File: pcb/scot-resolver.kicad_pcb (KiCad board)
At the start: 2 copper layers, 108.6 x 79.4 mm, 149 parts, among them IC1 AD8692ARMZ, IC10 AD2S1210, IC2 AD8397ARZ, IC3 AD8692ARMZ, IC4 TSR1, IC5 AD8692ARMZ, IC6 AD8692ARMZ, IC7 AD8692ARMZ, IC8 MCP2562, IC9 STM32F0xxKxTx, J1 Conn_01x02_Female, J2 Conn_01x02_Female, J3 Conn_01x02_Female, J4 Conn_01x03_Female, J5 Conn_01x03_Female, J6 Conn_01x03_Female, J7 CONN_01x03, P1 SWD, U1 MCP1703A-5002_SOT223, U2 LT1762, U3 MCP1703A-5002_SOT223, U4 MCP1703A-5002_SOT223, U5 MCP1703A-3302_SOT223, Y1 Crystal_GND24, Y2 Crystal

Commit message: pcb: WIP layout of v2.
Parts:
- removed C40, C52: 6n8, Capacitor_SMD:C_0402_1005Metric
- removed C47: 1u, Capacitor_SMD:C_0603_1608Metric_Pad1.05x0.95mm_HandSolder
- removed C48, C49: 100n, Capacitor_SMD:C_0402_1005Metric
- removed C50: 1n2, Capacitor_SMD:C_0402_1005Metric
- removed C51: 220p, Capacitor_SMD:C_0402_1005Metric
- removed D1: D, Diode_SMD:D_1206_3216Metric_Pad1.42x1.75mm_HandSolder
- removed IC5, IC7: AD8692ARMZ, agg:MSOP-8
- removed R23, R33: 2K, Resistor_SMD:R_0402_1005Metric
- removed R24, R34: 22K, Resistor_SMD:R_0402_1005Metric
- removed R25, R35: 4K7, Resistor_SMD:R_0402_1005Metric
- removed R31: 27K, Resistor_SMD:R_0402_1005Metric
- removed R32: 1K2, Resistor_SMD:R_0402_1005Metric
- added FB5: 600R@100M/1A, Inductor_SMD:L_0805_2012Metric_Pad1.15x1.40mm_HandSolder, F.Cu at (219.6, 133.6)
- added FB6: 600R@100M/1A, Inductor_SMD:L_0805_2012Metric_Pad1.15x1.40mm_HandSolder, F.Cu at (219.6, 130.6)
- added FB7: Ferrite_Bead_Small, Inductor_SMD:L_0805_2012Metric_Pad1.15x1.40mm_HandSolder, F.Cu at (99.1, 80.5)
- added J8: Conn_01x02_Female, TerminalBlock_TE-Connectivity:TerminalBlock_TE_282834-2_1x02_P2.54mm_Horizontal, F.Cu at (179.9, 81.8)
- added JP1: SolderJumper_2_Open, Jumper:SolderJumper-2_P1.3mm_Open_RoundedPad1.0x1.5mm, F.Cu at (97.2, 86.3)
- added JP2: SolderJumper_2_Open, Jumper:SolderJumper-2_P1.3mm_Open_RoundedPad1.0x1.5mm, F.Cu at (232.2, 127.6)
- added TP1: TestPoint_Alt, TestPoint:TestPoint_Bridge_Pitch7.62mm_Drill1.3mm, F.Cu at (180.6, 140.5)
- added TP2: TestPoint, TestPoint:TestPoint_Pad_D1.5mm, F.Cu at (180.0, 144.6)
- added TP3: TestPoint, TestPoint:TestPoint_Pad_D1.5mm, F.Cu at (183.6, 144.6)
- added TP4: TestPoint, TestPoint:TestPoint_Pad_D1.5mm, F.Cu at (187.1, 144.6)
- added TP5: TestPoint, TestPoint:TestPoint_Pad_D1.5mm, F.Cu at (190.7, 144.6)
- added U6: LM317_3PinPackage, Package_TO_SOT_SMD:SOT-223-3_TabPin2, F.Cu at (154.6, 46.5)
- C10, C12, C13, C15, C16, C17, C18, C19, C2, C3, C4, C42, C43, C44, C45, C46, C5, C55, C56, C59, C6, C60, C61, C62, C63, C65, C66, C67, C68, C69, C7, C9: footprint Capacitor_SMD:C_0402_1005Metric -> Capacitor_SMD:C_0603_1608Metric_Pad1.05x0.95mm_HandSolder
- C21, C29, C30, C31: value 1u -> 1u/6.5V
- C22: value 2u2 -> 4u7/50V; footprint Capacitor_SMD:C_0603_1608Metric_Pad1.05x0.95mm_HandSolder -> Capacitor_SMD:C_1206_3216Metric_Pad1.42x1.75mm_HandSolder
- C23, C32, C33: value 1u -> 1u/5V
- C24: value 10n -> 10n/50V; footprint Capacitor_SMD:C_0402_1005Metric -> Capacitor_SMD:C_0603_1608Metric_Pad1.05x0.95mm_HandSolder
- C25: value 1u -> 4u7/6.5V
- C26: value 4u7 -> 4u7/50V
- C27, C28: value 10u -> 4u7/6.5V
- C34: value 1u -> 1u/3.3V
- C35: value 1u -> 4u7/50V; footprint Capacitor_SMD:C_0603_1608Metric_Pad1.05x0.95mm_HandSolder -> Capacitor_SMD:C_1206_3216Metric_Pad1.42x1.75mm_HandSolder
- C36: value 100n -> 100n/50V; footprint Capacitor_SMD:C_0402_1005Metric -> Capacitor_SMD:C_0603_1608Metric_Pad1.05x0.95mm_HandSolder
- C37: value 100n -> 4u7/50V; footprint Capacitor_SMD:C_0402_1005Metric -> Capacitor_SMD:C_0603_1608Metric_Pad1.05x0.95mm_HandSolder
- C38: value 1n2 -> 4u7/5V; footprint Capacitor_SMD:C_0402_1005Metric -> Capacitor_SMD:C_0805_2012Metric_Pad1.15x1.40mm_HandSolder
- C39: value 220p -> 10u; footprint Capacitor_SMD:C_0402_1005Metric -> Capacitor_SMD:C_0603_1608Metric_Pad1.05x0.95mm_HandSolder
- C53: value 100n -> 100n/3V3; footprint Capacitor_SMD:C_0402_1005Metric -> Capacitor_SMD:C_0603_1608Metric_Pad1.05x0.95mm_HandSolder
- C54: value 100n -> 100n/5V; footprint Capacitor_SMD:C_0402_1005Metric -> Capacitor_SMD:C_0603_1608Metric_Pad1.05x0.95mm_HandSolder
- C57, C58: value 12p -> 8p; footprint Capacitor_SMD:C_0402_1005Metric -> Capacitor_SMD:C_0603_1608Metric_Pad1.05x0.95mm_HandSolder
- FB1, FB2, FB3, FB4: value Ferrite_Bead_Small -> 600R@100M/1A
- IC8: footprint agg:DFN-8-EP-MICROCHIP -> agg:SOIC-8
- J2, J3: value Conn_01x02_Female -> Conn_01x03_Female; footprint TerminalBlock_TE-Connectivity:TerminalBlock_TE_282834-2_1x02_P2.54mm_Horizontal -> TerminalBlock_TE-Connectivity:TerminalBlock_TE_282834-3_1x03_P2.54mm_Horizontal
- J5, J6: value Conn_01x03_Female -> Conn_01x02_Female; footprint TerminalBlock_TE-Connectivity:TerminalBlock_TE_282834-3_1x03_P2.54mm_Horizontal -> TerminalBlock_TE-Connectivity:TerminalBlock_TE_282834-2_1x02_P2.54mm_Horizontal
- R1, R11, R12, R14, R15, R16, R2, R27, R28, R29, R3, R39, R4, R5, R6, R7, R8: footprint Resistor_SMD:R_0402_1005Metric -> Resistor_SMD:R_0603_1608Metric_Pad1.05x0.95mm_HandSolder
- R10, R9: value 620R -> 390R; footprint Resistor_SMD:R_0402_1005Metric -> Resistor_SMD:R_0603_1608Metric_Pad1.05x0.95mm_HandSolder
- R13, R26: value 27K -> 120K; footprint Resistor_SMD:R_0402_1005Metric -> Resistor_SMD:R_0603_1608Metric_Pad1.05x0.95mm_HandSolder
- R17, R30: value 4K7 -> 2K7; footprint Resistor_SMD:R_0402_1005Metric -> Resistor_SMD:R_0603_1608Metric_Pad1.05x0.95mm_HandSolder
- R18: value R -> 68K
- R19: value R -> 5K6
- R21: value 27K -> 240R/1%; footprint Resistor_SMD:R_0402_1005Metric -> Resistor_SMD:R_0805_2012Metric_Pad1.15x1.40mm_HandSolder
- R22: value 1K2 -> 3K2/1%; footprint Resistor_SMD:R_0402_1005Metric -> Resistor_SMD:R_0805_2012Metric_Pad1.15x1.40mm_HandSolder
- moved C36 98.4 mm to (74.1, 64.2), turned to 0 degrees
- moved C38 71.9 mm to (227.6, 127.3), turned to 0 degrees
- moved C37 62.0 mm to (212.3, 138.5), turned to 0 degrees
- moved C35 57.4 mm to (215.5, 127.5), turned to 0 degrees
- moved R22 57.0 mm to (214.9, 130.6)
- moved R21 56.3 mm to (214.9, 133.6), turned to 0 degrees
- moved C39 22.3 mm to (149.6, 93.5), turned to 0 degrees
- moved J2 15.2 mm to (85.7, 83.6)
- moved J3 9.47 mm to (86.2, 96.1)
- moved J6 9.04 mm to (179.9, 93.4)
- moved J5 7.70 mm to (179.7, 104.6), turned to 90 degrees
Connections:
- net /Power Supplies/12V_EXCITER renamed /Power Supplies/EXCITER_16V+
- C20 pad 1: AVCC -> Net-(C20-Pad1)
- C20 pad 2: GNDA -> /Power Supplies/0V_EXCITER
- C21 pad 1: AVCC -> /Power Supplies/ANALOG_6.5V+
- C21 pad 2: GNDA -> /Power Supplies/0V_ANALOG
- C22 pad 1: Net-(C22-Pad1) -> /Power Supplies/POWER_28V+
- C23 pad 2: GNDA -> /Power Supplies/0V_ANALOG
- C24 pad 2: GNDA -> /Power Supplies/0V_EXCITER
- C26 pad 2: GNDA -> /Power Supplies/0V_EXCITER
- C27 pad 1: AVCC -> /Power Supplies/DIGITAL_6.5V+
- C27 pad 2: GNDA -> /Power Supplies/0V_DIGITAL
- C28 pad 1: +15V -> /Power Supplies/ANALOG_6.5V+
- C28 pad 2: GND -> /Power Supplies/0V_ANALOG
- C29 pad 1: +15V -> /Power Supplies/DIGITAL_6.5V+
- C29 pad 2: GND -> /Power Supplies/0V_DIGITAL
- C30 pad 1: +15V -> /Power Supplies/DIGITAL_6.5V+
- C30 pad 2: GND -> /Power Supplies/0V_DIGITAL
- C31 pad 1: +15V -> /Power Supplies/DIGITAL_6.5V+
- C31 pad 2: GND -> /Power Supplies/0V_DIGITAL
- C32 pad 2: GND -> /Power Supplies/0V_DIGITAL
- C33 pad 2: GND -> /Power Supplies/0V_DIGITAL
- C34 pad 2: GND -> /Power Supplies/0V_DIGITAL
- C35 pad 1: GNDA -> /Power Supplies/POWER_28V+
- C35 pad 2: /Microcontroller & Interface/5V_RESOLVER_ANALOGUE -> /Power Supplies/POWER_28V-
- C36 pad 1: GNDA -> /Power Supplies/POWER_28V+
- C36 pad 2: /Resolver Exciter/AD2S1210_VREF -> /Power Supplies/POWER_28V-
- C37 pad 1: GNDA -> Net-(C37-Pad1)
- C37 pad 2: /Microcontroller & Interface/5V_RESOLVER_ANALOGUE -> /Power Supplies/POWER_28V-
- C38 pad 1: Net-(C38-Pad1) -> GND
- C38 pad 2: /Resolver Receiver SIN-/AD2S1210_INPUT -> /CAN TXRX/5V_CAN
- C39 pad 1: Net-(C39-Pad1) -> /Resolver Exciter/AD2S1210_VREF
- C39 pad 2: Net-(C39-Pad2) -> GNDA
- C59 pad 1: /CAN TXRX/3.3V_MCU -> Net-(C59-Pad1)
- C66 pad 1: Net-(C66-Pad1) -> /Microcontroller & Interface/RD_nRESET
- D2 pad 2: +15V -> /Power Supplies/ANALOG_6.5V+
- FB1 pad 1: AVCC -> /Power Supplies/DIGITAL_6.5V+
- FB2 pad 2: GNDA -> /Power Supplies/0V_DIGITAL
- FB3 pad 1: AVCC -> /Power Supplies/DIGITAL_6.5V+
- FB3 pad 2: +15V -> /Power Supplies/ANALOG_6.5V+
- FB4 pad 1: GNDA -> /Power Supplies/0V_DIGITAL
- FB4 pad 2: GND -> /Power Supplies/0V_ANALOG
- IC10 pad 33: Net-(C66-Pad1) -> /Microcontroller & Interface/RD_nRESET
- IC10 pad 42: /Resolver Receiver SIN-/AD2S1210_INPUT -> /Resolver Exciter/AD2S1210_VREF
- IC10 pad 44: /Resolver Receiver COS-/AD2S1210_INPUT -> /Resolver Exciter/AD2S1210_VREF
- IC4 pad 1: Net-(C22-Pad1) -> /Power Supplies/POWER_28V+
- IC9 pad 29: Net-(IC9-Pad29) -> /Microcontroller & Interface/RD_nRESET
- IC9 pad 5: /CAN TXRX/3.3V_MCU -> Net-(C59-Pad1)
- J2 pad 1: /CAN TXRX/CAN_L -> Net-(J2-Pad1)
- J2 pad 2: /CAN TXRX/CAN_H -> /CAN TXRX/CAN_L
- J3 pad 1: /CAN TXRX/CAN_L -> Net-(J2-Pad1)
- J3 pad 2: /CAN TXRX/CAN_H -> /CAN TXRX/CAN_L
- J5 pad 2: /Resolver Receiver SIN-/RECEIVER_INPUT -> /Resolver Receiver SIN+/RECEIVER_INPUT
- J6 pad 2: /Resolver Receiver COS-/RECEIVER_INPUT -> /Resolver Exciter/AD2S1210_VREF
- R19 pad 2: GNDA -> /Power Supplies/0V_EXCITER
- R20 pad 2: GND -> /Power Supplies/0V_ANALOG
- R21 pad 1: /Resolver Receiver SIN-/RECEIVER_INPUT -> Net-(C37-Pad1)
- R21 pad 2: Net-(C39-Pad1) -> Net-(R21-Pad2)
- R22 pad 1: Net-(C38-Pad1) -> Net-(R21-Pad2)
- R22 pad 2: Net-(C40-Pad1) -> /Power Supplies/POWER_28V-
- R36 pad 1: /CAN TXRX/CAN_H -> Net-(JP2-Pad1)
- R39 pad 2: Net-(C66-Pad1) -> /Microcontroller & Interface/RD_nRESET
- U1 pad 1: AVCC -> /Power Supplies/ANALOG_6.5V+
- U1 pad 2: GNDA -> /Power Supplies/0V_ANALOG
- U2 pad 4: GNDA -> /Power Supplies/0V_EXCITER
- U2 pad 5: AVCC -> Net-(C20-Pad1)
- U2 pad 8: AVCC -> Net-(C20-Pad1)
- U3 pad 1: +15V -> /Power Supplies/DIGITAL_6.5V+
- U3 pad 2: GND -> /Power Supplies/0V_DIGITAL
- U4 pad 1: +15V -> /Power Supplies/DIGITAL_6.5V+
- U4 pad 2: GND -> /Power Supplies/0V_DIGITAL
- U5 pad 1: +15V -> /Power Supplies/DIGITAL_6.5V+
- U5 pad 2: GND -> /Power Supplies/0V_DIGITAL
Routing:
- net GNDA: track 462.5 -> 365.5 mm, vias 78 -> 73
- net +15V: track 59.2 -> 0.00 mm
- net /Power Supplies/DIGITAL_6.5V+: track 0.00 -> 49.2 mm
- net /Resolver Exciter/AD2S1210_VREF: track 179.2 -> 140.4 mm, vias 17 -> 10
- net /Resolver Receiver COS-/AD2S1210_INPUT: track 37.3 -> 0.00 mm
- net /CAN TXRX/3.3V_MCU: track 226.0 -> 191.5 mm
- net /Resolver Receiver SIN-/AD2S1210_INPUT: track 34.2 -> 0.00 mm
- net AVCC: track 84.9 -> 55.8 mm, vias 3 -> 2
- net /Microcontroller & Interface/5V_RESOLVER_ANALOGUE: track 193.4 -> 164.8 mm, vias 12 -> 8
- net Net-(JP2-Pad1): track 0.00 -> 22.9 mm
- net /CAN TXRX/CAN_H: track 22.9 -> 0.00 mm
- net Net-(C40-Pad1): track 14.0 -> 0.00 mm
- net Net-(C52-Pad1): track 13.2 -> 0.00 mm
- net /Power Supplies/0V_DIGITAL: track 0.00 -> 13.0 mm
- net /Resolver Receiver SIN-/RECEIVER_INPUT: track 7.40 -> 0.00 mm
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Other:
- board text added: "April 2020"
- board text removed: "Feb 2020"

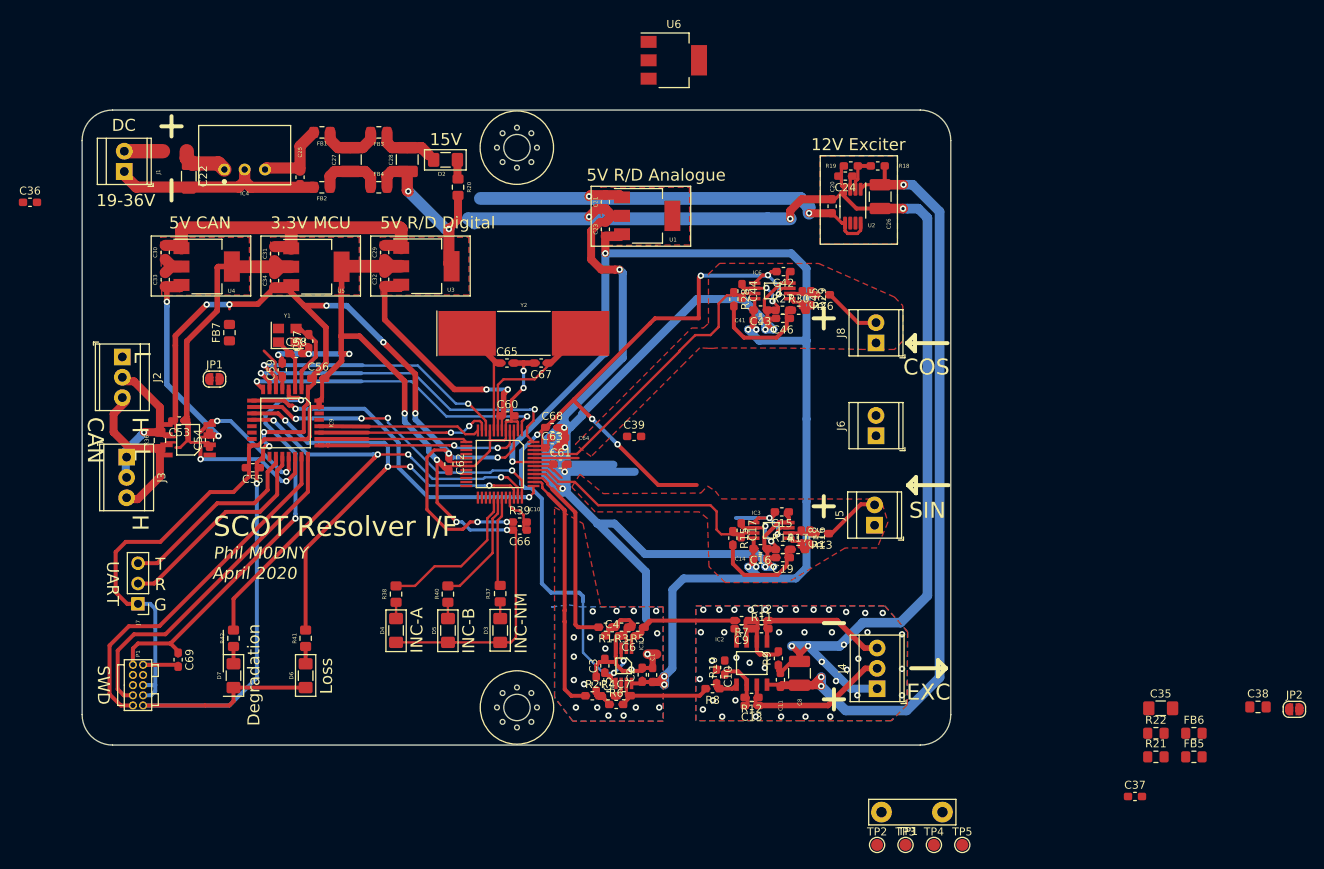
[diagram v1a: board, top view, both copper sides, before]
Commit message: pcb: Progress on v2 layout.
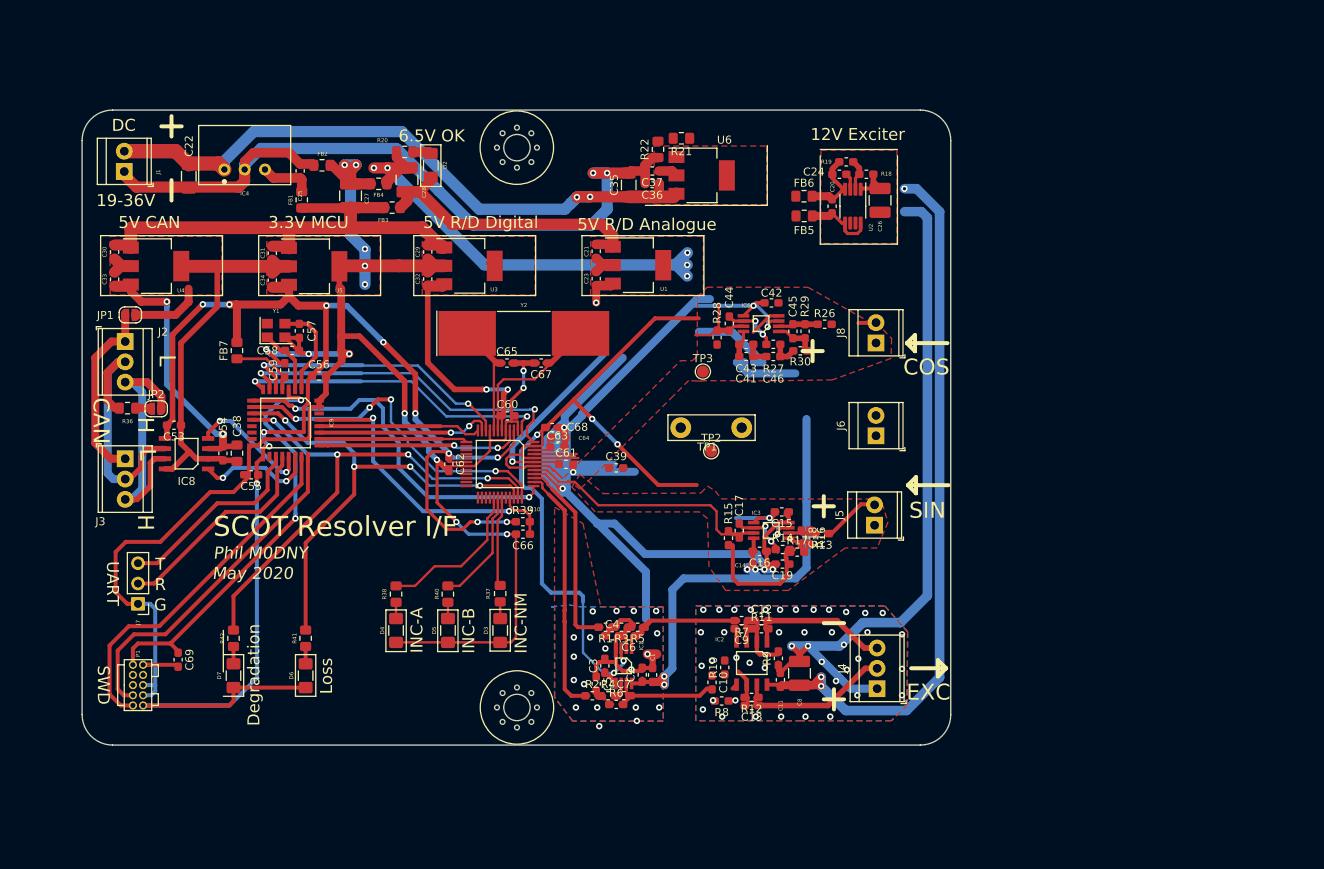
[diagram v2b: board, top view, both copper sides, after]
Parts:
- removed TP4, TP5: TestPoint, TestPoint:TestPoint_Pad_D1.5mm
- moved JP2 147.1 mm to (89.9, 90.0)
- moved C38 131.5 mm to (100.0, 95.6), turned to 90 degrees
- moved C37 98.8 mm to (151.9, 60.3), turned to 180 degrees
- moved R21 97.4 mm to (155.6, 56.2), turned to 180 degrees
- moved R22 95.9 mm to (152.6, 57.6), turned to 270 degrees
- moved C35 93.3 mm to (149.0, 62.1), turned to 90 degrees
- moved FB5 83.3 mm to (170.9, 65.9)
- moved FB6 83.0 mm to (170.9, 63.5)
- moved C36 77.8 mm to (151.9, 61.9), turned to 180 degrees
- moved TP3 64.4 mm to (158.2, 85.4)
- moved TP1 54.2 mm to (155.5, 92.4)
- moved TP2 53.4 mm to (159.3, 95.4)
- moved U6 14.8 mm to (158.1, 60.9)
- moved JP1 13.2 mm to (86.7, 78.3)
- moved FB3 9.54 mm to (119.4, 64.9)
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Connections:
- C21 pad 2: /Power Supplies/0V_ANALOG -> GNDA
- C23 pad 2: /Power Supplies/0V_ANALOG -> GNDA
- C27 pad 2: /Power Supplies/0V_DIGITAL -> GND
- C28 pad 2: /Power Supplies/0V_ANALOG -> GNDA
- C29 pad 2: /Power Supplies/0V_DIGITAL -> GND
- C30 pad 2: /Power Supplies/0V_DIGITAL -> GND
- C31 pad 2: /Power Supplies/0V_DIGITAL -> GND
- C32 pad 2: /Power Supplies/0V_DIGITAL -> GND
- C33 pad 2: /Power Supplies/0V_DIGITAL -> GND
- C34 pad 2: /Power Supplies/0V_DIGITAL -> GND
- FB2 pad 2: /Power Supplies/0V_DIGITAL -> GND
- FB4 pad 1: /Power Supplies/0V_DIGITAL -> GND
- FB4 pad 2: /Power Supplies/0V_ANALOG -> GNDA
- R20 pad 2: /Power Supplies/0V_ANALOG -> GNDA
- U1 pad 2: /Power Supplies/0V_ANALOG -> GNDA
- U3 pad 2: /Power Supplies/0V_DIGITAL -> GND
- U4 pad 2: /Power Supplies/0V_DIGITAL -> GND
- U5 pad 2: /Power Supplies/0V_DIGITAL -> GND
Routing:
- net /Power Supplies/POWER_28V-: track 26.8 -> 97.4 mm, vias 0 -> 2
- net /Power Supplies/POWER_28V+: track 11.0 -> 81.5 mm, vias 0 -> 2
- net /Microcontroller & Interface/5V_RESOLVER_ANALOGUE: track 164.8 -> 105.2 mm, vias 8 -> 6
- net AVCC: track 55.8 -> 0.00 mm, vias 2 -> 0
- net GND: track 276.0 -> 319.7 mm, vias 11 -> 14
- net GNDA: track 365.5 -> 328.2 mm, vias 73 -> 70
- net /Microcontroller & Interface/RD_nRESET: track 5.12 -> 38.8 mm, vias 0 -> 2
- net /CAN TXRX/CAN_H: track 0.00 -> 33.0 mm
- net /Power Supplies/ANALOG_6.5V+: track 7.10 -> 36.3 mm
- net Net-(J2-Pad1): track 0.00 -> 23.1 mm
- net /Resolver Receiver COS+/AD2S1210_INPUT: track 37.7 -> 15.2 mm
- net Net-(JP2-Pad1): track 22.9 -> 1.94 mm
- net /Power Supplies/DIGITAL_6.5V+: track 49.2 -> 64.7 mm
- net /CAN TXRX/CAN_L: track 19.7 -> 33.4 mm, vias 1 -> 0
- net /Power Supplies/0V_DIGITAL: track 13.0 -> 0.00 mm
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- added copper zone on F.Cu, net Net-(C37-Pad1)
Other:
- board text added: "6.5V OK"
- board text added: "May 2020"
- board text removed: "15V"
- board text removed: "April 2020"

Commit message: pcb: Clear up exciter ground rail (sch & pcb).
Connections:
- C10 pad 1: GNDA -> /Power Supplies/0V_EXCITER
- C11 pad 2: GNDA -> /Power Supplies/0V_EXCITER
- C8 pad 2: GNDA -> /Power Supplies/0V_EXCITER
- C9 pad 2: GNDA -> /Power Supplies/0V_EXCITER
- IC2 pad 4: GNDA -> /Power Supplies/0V_EXCITER
- J4 pad 1: GNDA -> /Power Supplies/0V_EXCITER
- R10 pad 2: GNDA -> /Power Supplies/0V_EXCITER
- R9 pad 1: GNDA -> /Power Supplies/0V_EXCITER
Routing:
- net /Power Supplies/0V_EXCITER: track 8.96 -> 100.5 mm, vias 0 -> 4
- net GNDA: track 328.2 -> 236.6 mm, vias 70 -> 66

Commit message: pcb: Progress on layout.
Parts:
- moved C39 28.3 mm to (175.2, 92.2), turned to 270 degrees
- moved TPe 8.97 mm to (156.8, 104.0)
- moved TP1 4.63 mm to (159.9, 93.8)
- moved R13 3.79 mm to (174.0, 102.0)
- moved C14 3.65 mm to (163.8, 106.3)
- moved TP3 3.64 mm to (154.6, 85.4)
- moved C16 3.42 mm to (163.8, 104.8)
- moved C15 3.33 mm to (167.5, 99.6)
- moved C18 3.30 mm to (170.0, 102.9)
- moved C19 3.30 mm to (167.2, 106.3)
- moved R16 3.25 mm to (171.5, 102.9)
- moved C17 3.12 mm to (162.0, 102.2)
- moved IC3 3.12 mm to (166.0, 102.2)
- moved R14 3.02 mm to (167.2, 104.8)
- moved R17 2.68 mm to (170.5, 105.3)
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- renumbered TP2 to TPe
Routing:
- net /Power Supplies/POWER_28V-: track 97.4 -> 127.6 mm
- net GNDA: track 236.6 -> 220.2 mm, vias 66 -> 37
- net Net-(C37-Pad1): track 2.39 -> 10.8 mm
- net Net-(R21-Pad2): track 0.00 -> 6.00 mm
- net /Resolver Receiver SIN+/RECEIVER_INPUT: track 7.50 -> 1.59 mm
- net /Resolver Receiver SIN+/AD2S1210_INPUT: track 32.3 -> 27.5 mm
- net /Resolver Receiver COS+/AD2S1210_INPUT: track 15.2 -> 10.9 mm
- net Net-(C10-Pad2): track 0.71 -> 5.00 mm
- net /Power Supplies/0V_EXCITER: track 100.5 -> 104.6 mm, vias 4 -> 50
- net Net-(C5-Pad2): track 2.35 -> 5.96 mm
- net Net-(C4-Pad1): track 5.42 -> 8.55 mm
- net /Power Supplies/EXCITER_16V+: track 97.4 -> 100.5 mm
- net /Resolver Exciter/AD2S1210_EXC+: track 31.4 -> 28.4 mm
- net Net-(C13-Pad2): track 4.76 -> 7.59 mm
- net /Microcontroller & Interface/5V_RESOLVER_ANALOGUE: track 105.2 -> 102.4 mm
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- added copper zone on B.Cu, net /Power Supplies/0V_EXCITER
- added copper zone on F.Cu, net /Power Supplies/0V_EXCITER
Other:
- board text added: "18V->16V Exciter"
- board text added: "VREF"
- board text removed: "12V Exciter"

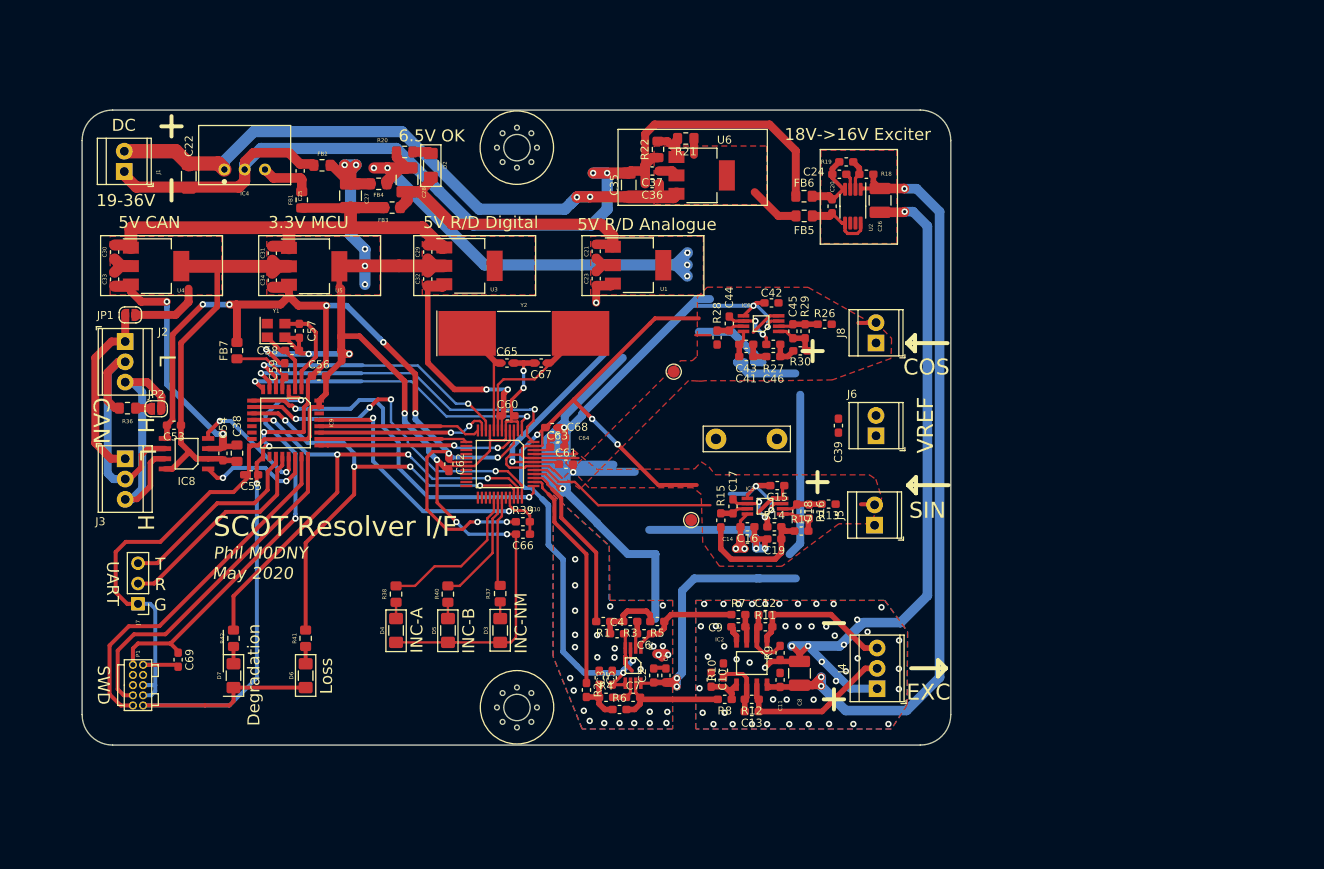
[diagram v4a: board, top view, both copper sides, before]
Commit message: pcb: Finish v2 and send off for manufacture.
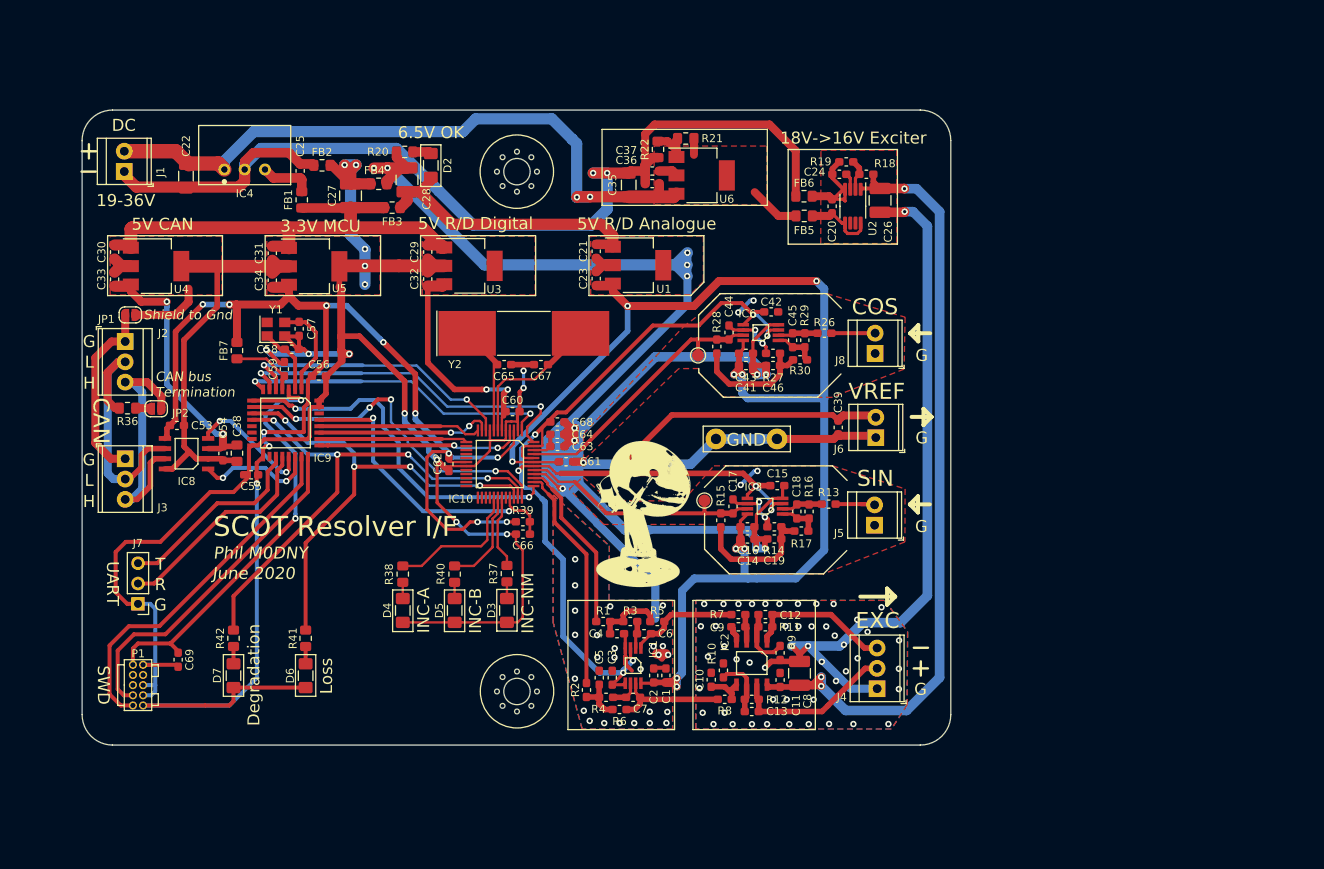
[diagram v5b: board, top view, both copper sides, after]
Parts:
- added G***: LOGO, scot_logo:scot_logo, F.Cu at (150.8, 103.2)
- moved TP3 3.66 mm to (157.6, 83.4)
- moved H1 3.00 mm to (135.0, 60.4)
- moved TPe 2.95 mm to (158.4, 101.5)
- moved D3 2.64 mm to (133.7, 115.3)
- moved R37 2.64 mm to (133.7, 110.6)
- moved R40 2.64 mm to (127.2, 110.7)
- moved D4 2.64 mm to (120.7, 115.3)
- moved D5 2.64 mm to (127.2, 115.3)
- moved R38 2.64 mm to (120.7, 110.7)
- moved H2 2.00 mm to (135.0, 125.4)
- moved J8 1.32 mm to (179.8, 83.1)
- moved C41 1.12 mm to (163.6, 84.6)
- moved C42 1.12 mm to (166.8, 77.9)
- moved C44 1.12 mm to (161.5, 80.5)
- moved C46 1.12 mm to (167.0, 84.6)
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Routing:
- net GNDA: track 220.2 -> 292.8 mm, vias 37 -> 42
- net /Microcontroller & Interface/5V_RESOLVER_ANALOGUE: track 102.4 -> 166.0 mm, vias 6 -> 9
- net /Resolver Exciter/AD2S1210_VREF: track 146.7 -> 173.7 mm, vias 9 -> 8
- net /Resolver Receiver COS+/AD2S1210_INPUT: track 10.9 -> 34.4 mm
- net Net-(C46-Pad1): track 3.44 -> 15.9 mm
- net /Resolver Receiver SIN+/RECEIVER_INPUT: track 1.59 -> 5.55 mm
- net /Resolver Receiver COS+/RECEIVER_INPUT: track 1.84 -> 5.47 mm
- net /Resolver Receiver SIN+/AD2S1210_INPUT: track 27.5 -> 30.9 mm
- net /Power Supplies/0V_EXCITER: track 104.6 -> 107.8 mm
- net GND: track 319.7 -> 316.6 mm
- net /Power Supplies/POWER_28V+: track 81.5 -> 84.5 mm
- net /Microcontroller & Interface/INC_B: track 14.5 -> 12.2 mm
- net /Microcontroller & Interface/INC_A: track 19.4 -> 17.5 mm
- net /Microcontroller & Interface/INC_NM: track 11.3 -> 9.62 mm
- net /Microcontroller & Interface/RES0: track 43.4 -> 44.7 mm
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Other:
- board text added: "CAN bus Termination"
- board text added: "GND"
- board text added: "June 2020"
- board text added: "Shield to Gnd"
- board text removed: "May 2020"
